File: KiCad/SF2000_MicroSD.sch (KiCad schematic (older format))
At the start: 5 parts, among them J6 Micro_SD_Card_Socket, X1 Oscillator_7.0x5.0mm

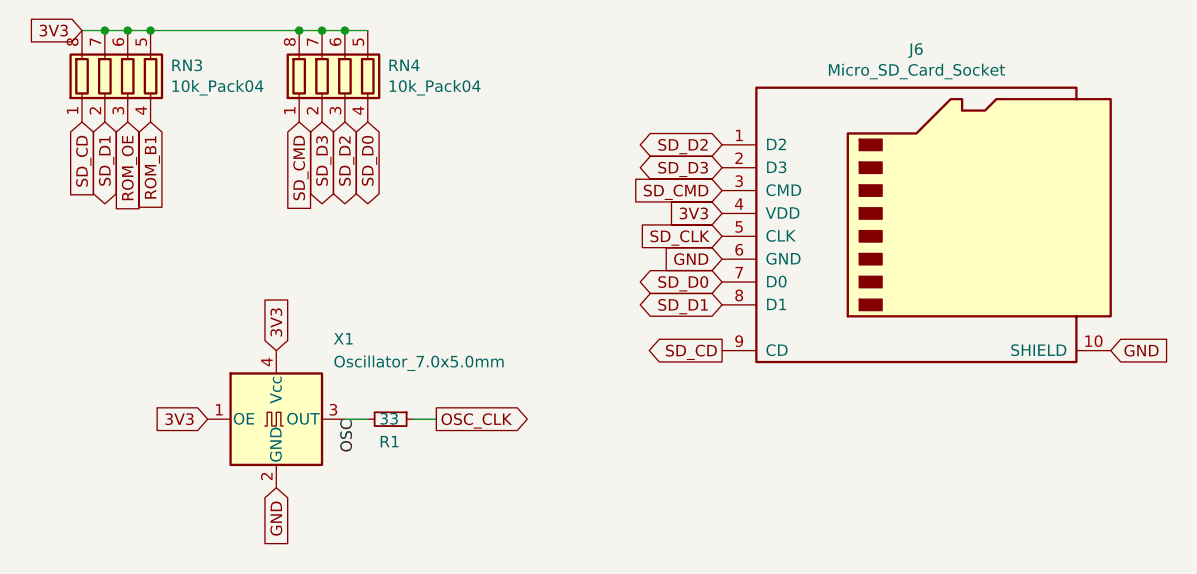
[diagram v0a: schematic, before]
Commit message: Fix of SD-card control signals and routing
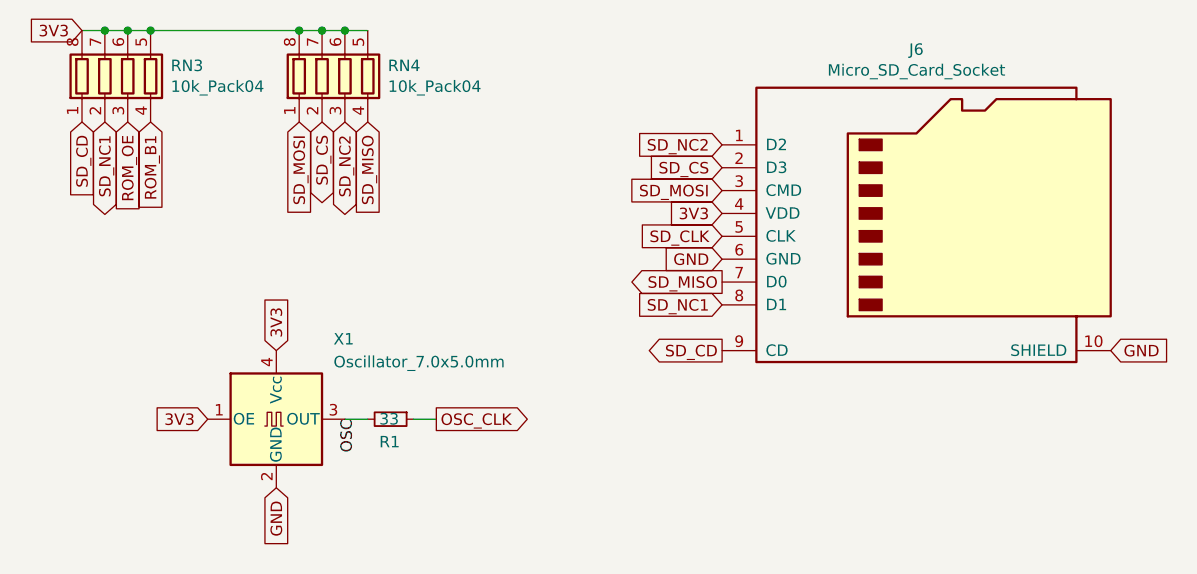
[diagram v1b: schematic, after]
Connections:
- net SD_CMD renamed SD_MOSI
- net SD_D0 renamed SD_MISO
- net SD_D1 renamed SD_NC1
- net SD_D2 renamed SD_NC2
- net SD_D3 renamed SD_CS
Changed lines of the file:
@@
 	1    0    0    -1
 $EndComp
-Text GLabel 4800 3900 0    50   BiDi ~ 0
-SD_D0
-Text GLabel 4800 4000 0    50   BiDi ~ 0
-SD_D1
-Text GLabel 4800 3300 0    50   BiDi ~ 0
-SD_D2
-Text GLabel 4800 3400 0    50   BiDi ~ 0
-SD_D3
+Text GLabel 4800 3900 0    50   Output ~ 0
+SD_MISO
+Text GLabel 4800 4000 0    50   Input ~ 0
+SD_NC1
+Text GLabel 4800 3300 0    50   Input ~ 0
+SD_NC2
+Text GLabel 4800 3400 0    50   Input ~ 0
+SD_CS
 Text GLabel 4800 3500 0    50   Input ~ 0
-SD_CMD
+SD_MOSI
 Text GLabel 4800 3600 0    50   Input ~ 0
 3V3
@@
 	3150 2800 3250 2800
 Text GLabel 3150 3200 3    50   BiDi ~ 0
-SD_D2
+SD_NC2
 Text GLabel 3050 3200 3    50   BiDi ~ 0
-SD_D3
+SD_CS
 Text GLabel 2950 3200 3    50   Input ~ 0
-SD_CMD
-Text GLabel 3250 3200 3    50   BiDi ~ 0
-SD_D0
+SD_MOSI
+Text GLabel 3250 3200 3    50   Input ~ 0
+SD_MISO
 Text GLabel 2100 3200 3    50   BiDi ~ 0
-SD_D1
+SD_NC1
 Text GLabel 2000 3200 3    50   Input ~ 0
 SD_CD

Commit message: Fix continuous enumeration for pin-headers (J1 to J12)
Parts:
- renumbered J6 to J8
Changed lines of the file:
@@
 $EndDescr
 $Comp
-L SF2000:Micro_SD_Card_Socket J6
+L SF2000:Micro_SD_Card_Socket J8
 U 1 1 6289341C
 P 5700 3600
-F 0 "J6" H 5650 4317 50  0000 C CNN
+F 0 "J8" H 5650 4317 50  0000 C CNN
 F 1 "Micro_SD_Card_Socket" H 5650 4226 50  0000 C CNN
 F 2 "SF2000:GCT-MEM2055-00-190-01-A" H 6850 3900 50  0001 C CNN
